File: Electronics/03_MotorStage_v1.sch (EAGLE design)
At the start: 77 parts, among them J1 BARRIER_BLOCK-2PIN, J2 BARRIER_BLOCK-5PIN, J3 CONN_2X3_SMD, U1 XL4016-DEV

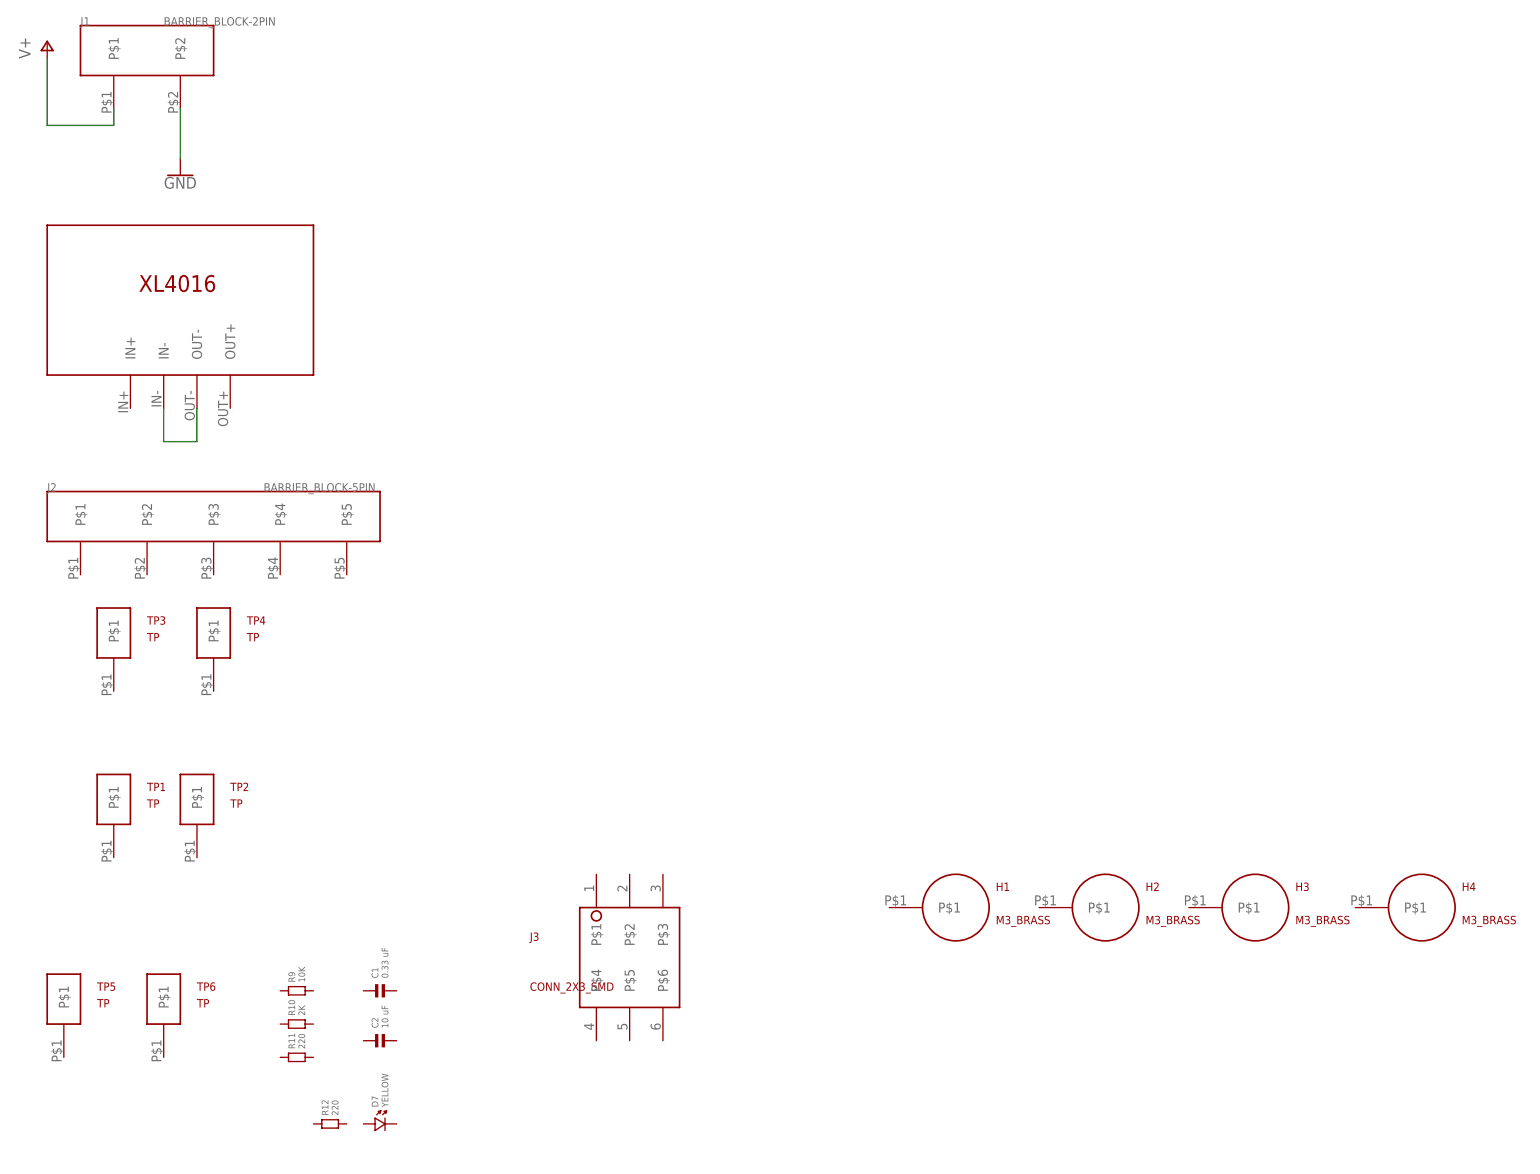
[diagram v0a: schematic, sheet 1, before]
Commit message: Completed routing of components on motor stage power supply board
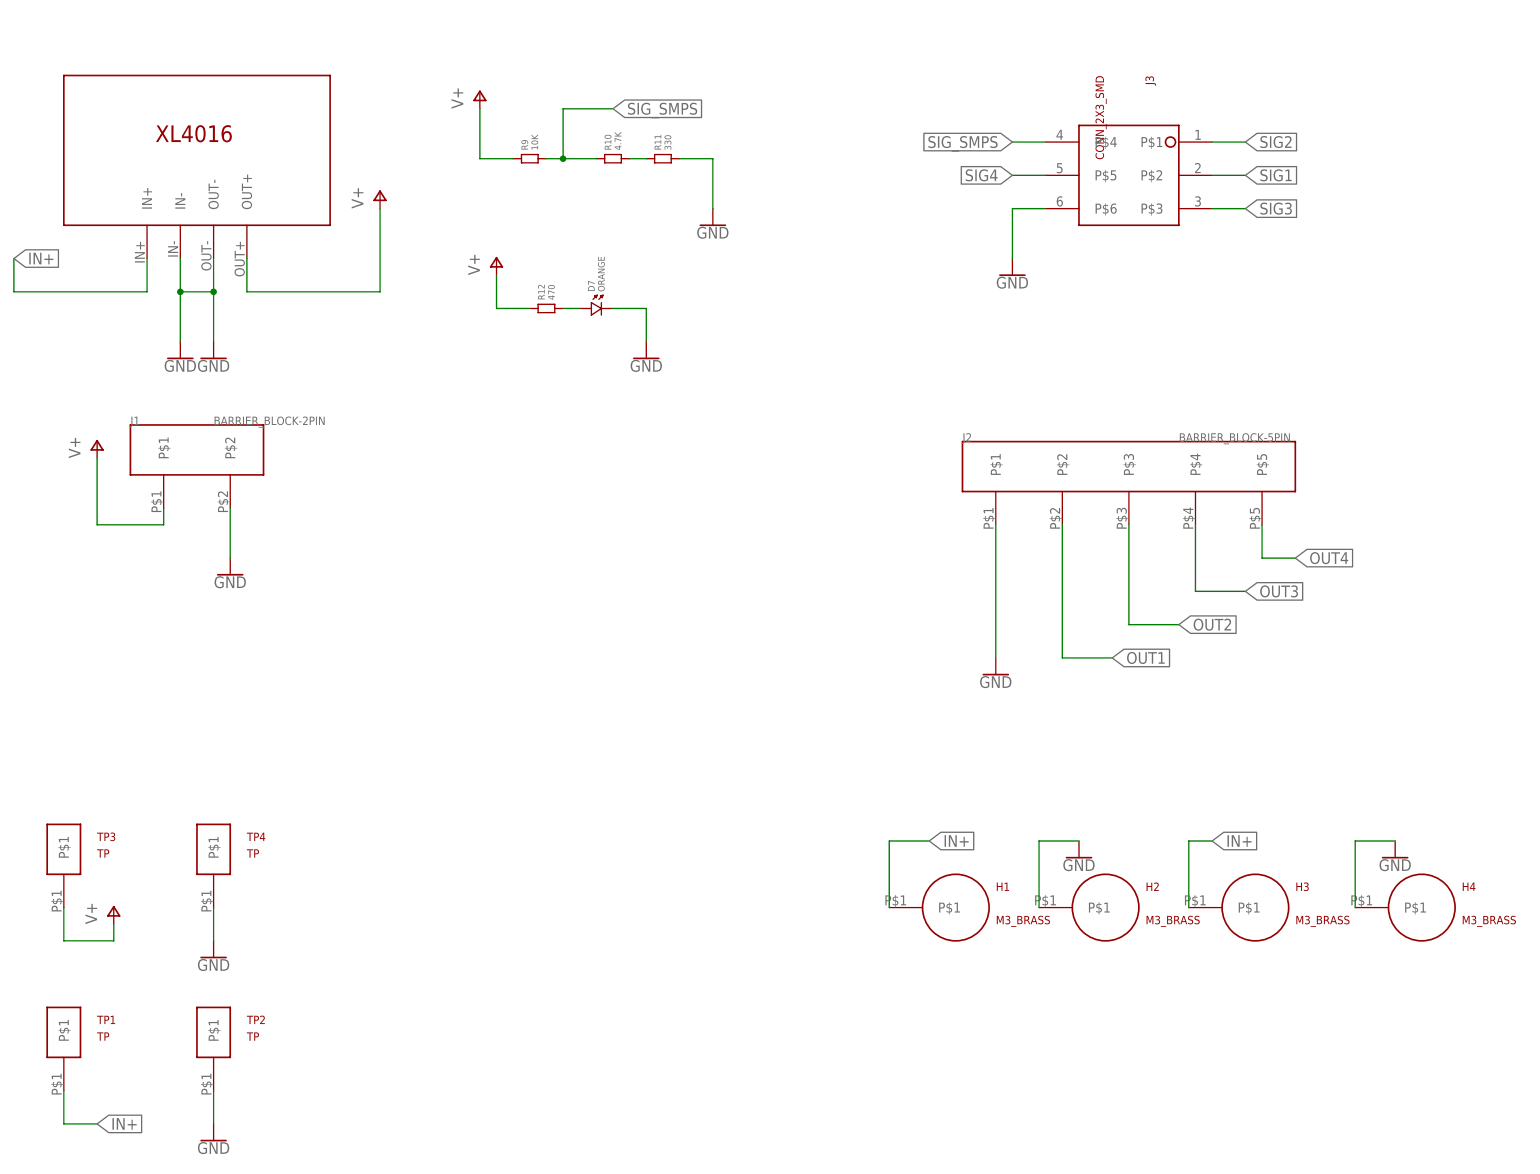
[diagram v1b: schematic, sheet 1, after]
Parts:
- removed C1: 0.33 uF, standardparts:CAPACITOR.1206
- removed C2: 10 uF, standardparts:CAPACITOR.1206
- removed TP5, TP6: TP, Hippo-PS:TP
- C10, C4, C6, C8: value (none) -> 22 uF
- C3, C5, C7, C9: value (none) -> 10 uF
- D7: value YELLOW -> ORANGE
- R10: value 2K -> 4.7K
- R11: value 220 -> 330
- R12: value 220 -> 470
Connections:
- removed net N$2: U1.IN-, U1.OUT-
- new net IN+: H1.P$1, H3.P$1, TP1.P$1, U1.IN+
- new net N$1: D7.1, R12.2
- new net N$23: R10.2, R11.1
- new net SIG_SMPS: J3.P$4, R10.1, R9.2
- net GND: now also D7.2, H2.P$1, H4.P$1, J2.P$1, J3.P$6, R11.2, TP2.P$1, TP4.P$1, U1.IN-, U1.OUT-
- net OUT1: now also J2.P$2
- net OUT2: now also J2.P$3
- net OUT3: now also J2.P$4
- net OUT4: now also J2.P$5
- net SIG1: now also J3.P$2
- net SIG2: now also J3.P$1
- net SIG3: now also J3.P$3
- net SIG4: now also J3.P$5
- net V+: now also R12.1, R9.1, TP3.P$1, U1.OUT+
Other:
- moved on the sheet: D7, J1, J2, J3, R10, R11, R12, R9, TP1, TP2, TP3, TP4
